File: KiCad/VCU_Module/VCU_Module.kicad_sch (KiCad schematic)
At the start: 46 parts, among them J1 5810132011, J10 12V, J12 MCU1, J13 MCU2, J14 5V, J15 3V3, J16 MCU3, J17 MCU4, J2 CN1, J3 CN2, J4 CN3, J5 MCU6, J6 CN4, J7 MCU5, J9 GND, Q1 AO3401A, U3 LMR33640DDDA, U4 LMR33640DDDA

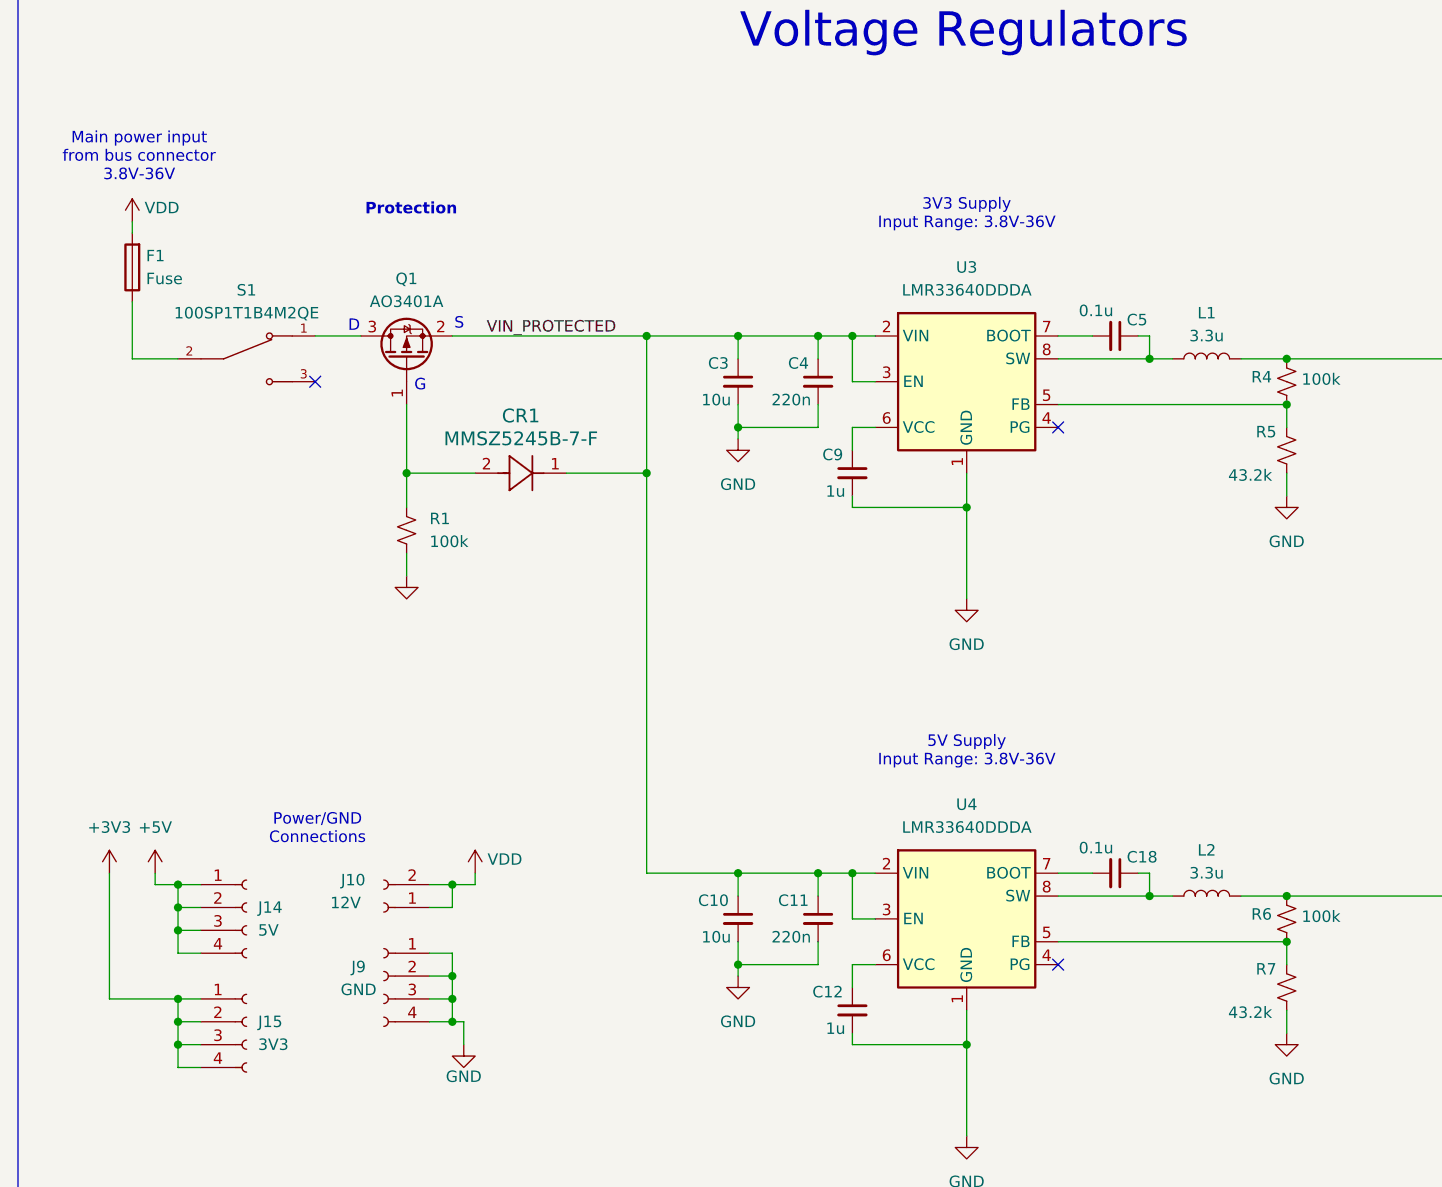
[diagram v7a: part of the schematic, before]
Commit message: Reapply "Modify power schematic to fix protection circuit as well as 5V buck regulator circuit"
This reverts commit ed7789357b0451a30a57dedadf80f61adec4e840.
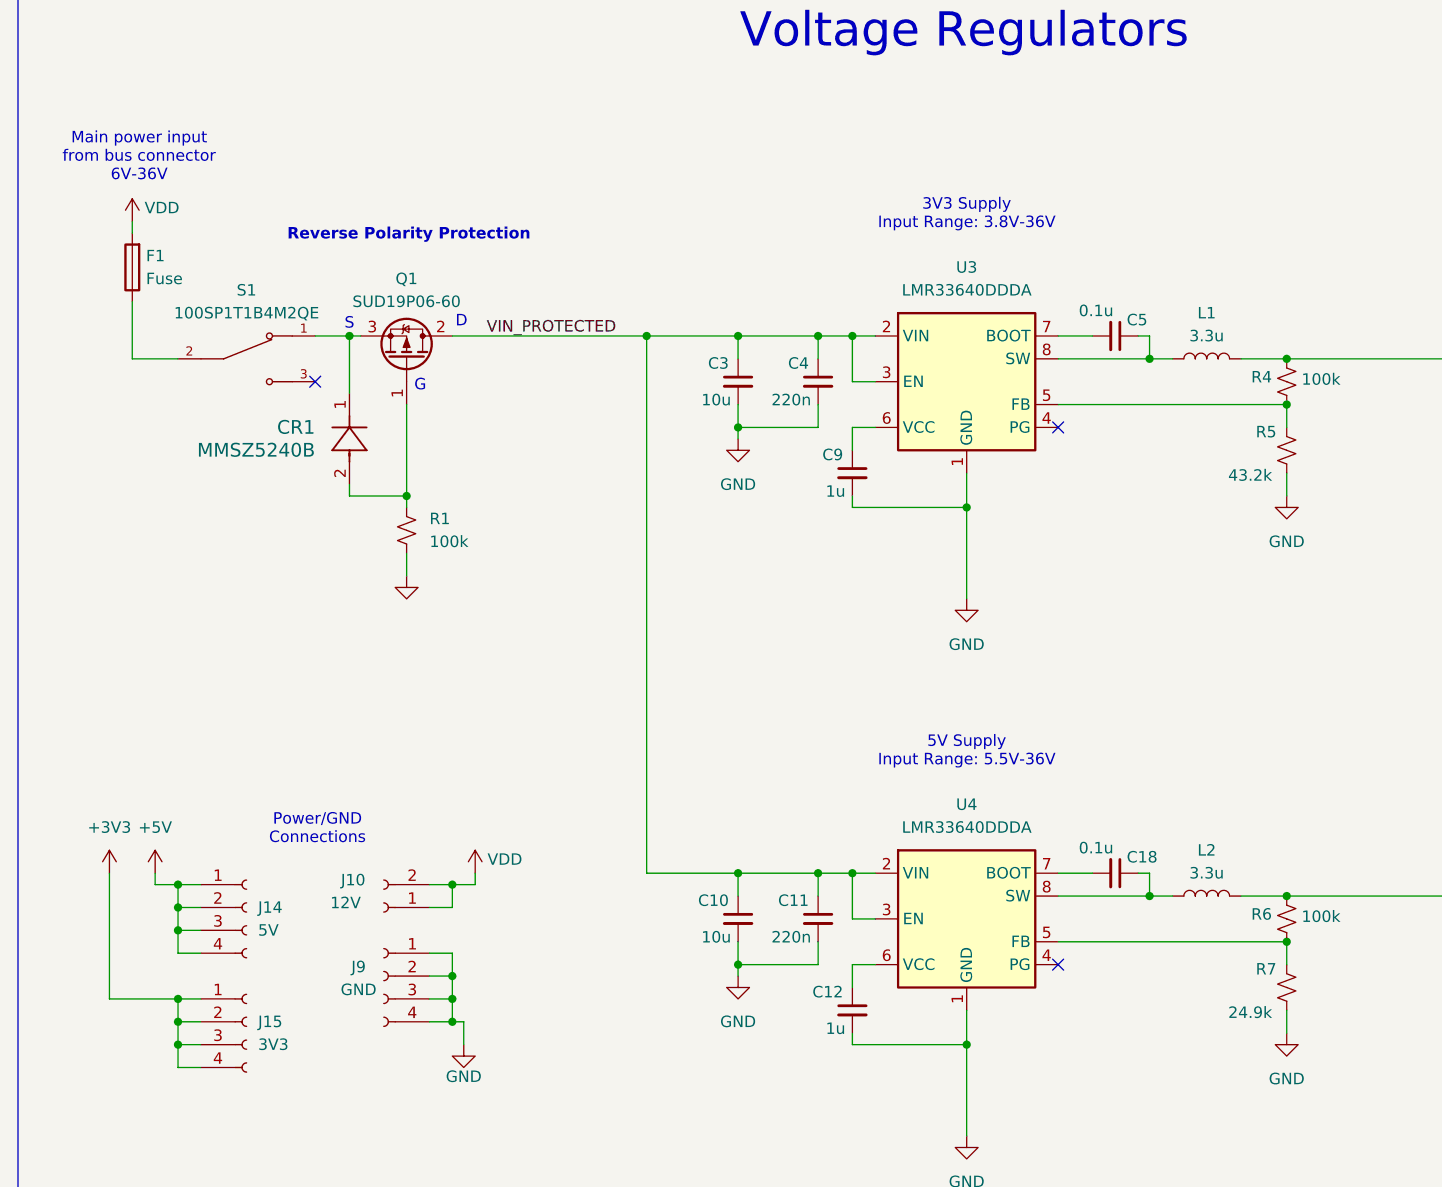
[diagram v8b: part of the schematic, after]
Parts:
- removed Q1: AO3401A, Package_TO_SOT_SMD:SOT-23, symbol Transistor_FET:AO3401A
- added Q1: SUD19P06-60, Package_TO_SOT_SMD:TO-252-2, symbol Transistor_FET:SUD19P06-60
- CR1: value MMSZ5245B-7-F -> MMSZ5240B; MPN MMSZ5245B-7-F -> MMSZ5240B; Purchase Link https://www.digikey.com/en/products/detail/diodes-incorpora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 -> (none)
- R7: value 43.2k -> 24.9k
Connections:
- net VIN_PROTECTED: now also Q1.2 (D); no longer CR1.1
- net at CR1.2, R1.1: now also Q1.1 (G)
- net at S1.1: now also CR1.1, Q1.3 (S)
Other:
- note added: "5V Supply Input Range: 5.5V-36V"
- note added: "Main power input from bus connector 6V-36V"
- note added: "Reverse Polarity Protection"
- note removed: "5V Supply Input Range: 3.8V-36V"
- note removed: "Main power input from bus connector 3.8V-36V"
- note removed: "Protection"
- moved on the sheet: CR1
